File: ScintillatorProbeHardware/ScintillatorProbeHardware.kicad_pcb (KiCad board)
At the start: 2 copper layers, 100 x 100 mm, 116 parts, among them J2 Conn_01x02, J3 Conn_01x03, J4 Conn_01x04, J7 Conn_01x02, Q1 15N10, Q2 S8050, Q3 S8050, Q4 AO401, Q5 S8050, Q6 S8050, Q7 S8050, T1 24:1800, U1 ICL7660, U3 LM358, U4 STM32F103C8Tx, U5 USBLC6-2SC6, U6 AMS1117-3.3, U7 LM318N, U8 LM318N, U9 LM318N, Y1 32.768kHz, Y2 8MHz

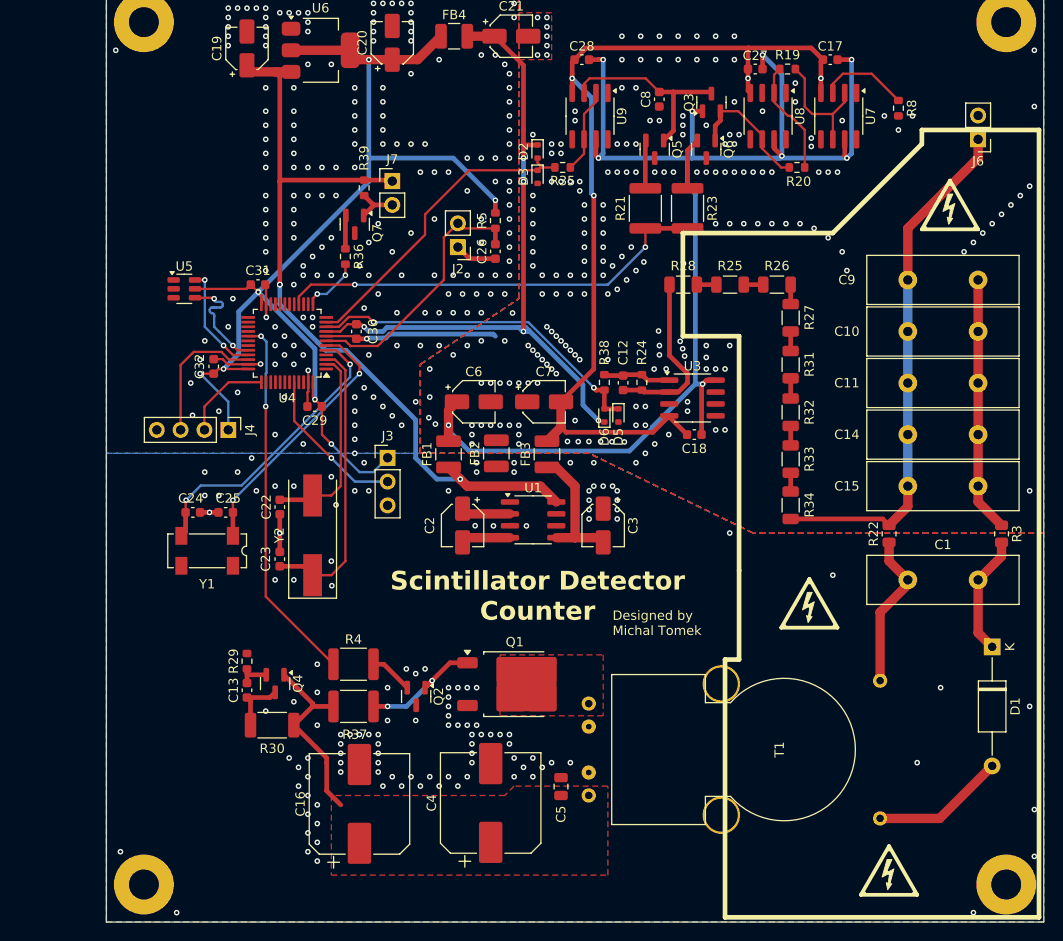
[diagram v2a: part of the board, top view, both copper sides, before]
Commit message: Added USB connector, some loops on PCB optimized
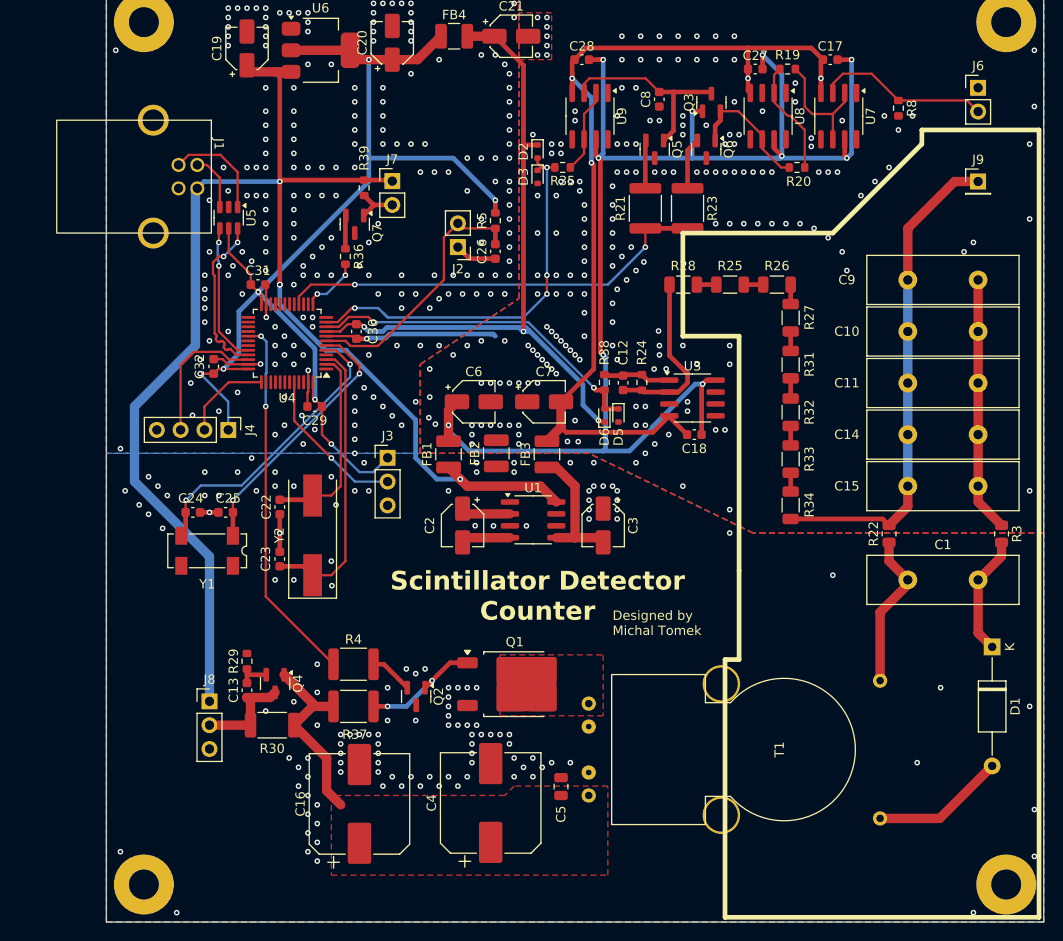
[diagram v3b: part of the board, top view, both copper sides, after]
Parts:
- removed REF** (x7): Symbol_HighVoltage_Triangle_6x6mm_Copper, Symbol:Symbol_HighVoltage_Triangle_6x6mm_Copper
- added J1: USB_B, CustomParts:Amphenol_USB_B, F.Cu at (149.7, 75.2)
- added J8: Conn_01x03, Connector_PinHeader_2.54mm:PinHeader_1x03_P2.54mm_Vertical, F.Cu at (153.0, 132.5)
- added J9: Conn_01x01, Connector_PinHeader_2.54mm:PinHeader_1x01_P2.54mm_Vertical, F.Cu at (235.0, 77.0)
- moved U5 8.95 mm to (155.1, 80.9), turned to -90 degrees
- moved J6 5.50 mm to (235.0, 67.0), turned to 0 degrees
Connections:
- J6 pad 1: HT -> GNDA
- U5 pad 1: Net-(J1-D+) -> /usb_P
- U5 pad 3: Net-(J1-D-) -> /usb_N
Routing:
- net +5V: track 84.5 -> 154.4 mm, vias 3 -> 4
- net /usb_P: track 0.00 -> 11.2 mm
- net Peak_Sense: track 33.7 -> 43.0 mm, vias 0 -> 4
- net PMT_Anode: track 9.60 -> 18.6 mm
- net +5VA: track 145.3 -> 152.5 mm, vias 9 -> 10
- net USB_D+: track 11.9 -> 18.0 mm
- net /usb_N: track 0.00 -> 6.09 mm
- net HT_Power: track 6.33 -> 10.7 mm
- net USB_D-: track 11.9 -> 15.1 mm
- net HT: track 55.9 -> 52.9 mm
- net +3.3V: track 124.1 -> 124.9 mm
- net GNDA: vias 209 -> 200
- net GND: vias 310 -> 334
- net +3.3VA: vias 5 -> 3

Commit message: Hardware finisnig touches, Software directory typo fixed
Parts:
- removed J5: ~, Connector_PinHeader_2.54mm:PinHeader_1x02_P2.54mm_Vertical
- removed R1, R2: 620k, Resistor_SMD:R_1218_3246Metric
- removed R10, R11, R12, R13, R14, R15, R16, R17, R18, R6, R9: 240k, Resistor_SMD:R_1206_3216Metric
- removed R7: 336k, Resistor_SMD:R_1206_3216Metric
- removed V1: ~, CustomParts:BDEG4-42A
- added J10: Conn_01x04, Connector_PinHeader_2.54mm:PinHeader_1x04_P2.54mm_Vertical, F.Cu at (147.5, 89.9)
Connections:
- U4 pad 30: unconnected-(U4-PA9-Pad30) -> UART_TX
- U4 pad 31: unconnected-(U4-PA10-Pad31) -> UART_RX
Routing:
- net UART_RX: track 0.00 -> 11.6 mm, vias 0 -> 1
- net UART_TX: track 0.00 -> 11.2 mm, vias 0 -> 1
- net /usb_P: track 11.2 -> 10.5 mm
- net GNDA: vias 200 -> 224
- net GND: vias 334 -> 361
- net -5VA: vias 4 -> 3
- net (no net): vias 0 -> 1

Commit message: Hardware revision 1 as sent to manifacture
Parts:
- removed Q4: AO401, Package_TO_SOT_SMD:SOT-23
- removed U5: USBLC6-2SC6, Package_TO_SOT_SMD:SOT-23-6
- added C33: 1u, Capacitor_SMD:C_0603_1608Metric, F.Cu at (195.7, 80.2)
- added C34: 1u, Capacitor_SMD:C_0603_1608Metric, F.Cu at (193.0, 80.2)
- added C35: 1u, Capacitor_SMD:C_0603_1608Metric, F.Cu at (223.7, 63.5)
- added C36: 1u, Capacitor_SMD:C_0603_1608Metric, F.Cu at (214.2, 61.2)
- added C37: 1u, Capacitor_SMD:C_0603_1608Metric, F.Cu at (214.0, 76.3)
- added C38: 1u, Capacitor_SMD:C_0603_1608Metric, F.Cu at (203.0, 64.2)
- added Q8: MDD2302, Package_TO_SOT_SMD:SOT-23, F.Cu at (160.6, 138.6)
- added R40: 1k, Resistor_SMD:R_0603_1608Metric, F.Cu at (167.7, 125.5)
- added SYM1: SYM_Flash_Small, CustomParts:W012 - electricity hazard, B.Cu at (228.6, 80.3)
- added SYM2: SYM_Flash_Small, CustomParts:W012 - electricity hazard, B.Cu at (217.0, 120.0)
- added SYM3: SYM_Flash_Small, CustomParts:W012 - electricity hazard, B.Cu at (231.5, 146.0)
- added SYM4: SYM_Flash_Small, CustomParts:W012 - electricity hazard, F.Cu at (228.6, 80.3)
- added SYM5: SYM_Flash_Small, CustomParts:W012 - electricity hazard, F.Cu at (217.0, 120.0)
- added SYM6: SYM_Flash_Small, CustomParts:W012 - electricity hazard, F.Cu at (231.5, 146.0)
- R21, R23: footprint Resistor_SMD:R_1812_4532Metric -> Resistor_SMD:R_0603_1608Metric
- R30: footprint Resistor_SMD:R_2010_5025Metric -> Resistor_SMD:R_0805_2012Metric
- R37, R4: footprint Resistor_SMD:R_1812_4532Metric -> Resistor_SMD:R_2010_5025Metric
- moved R29 12.8 mm to (156.7, 141.0), turned to 180 degrees
- moved R20 12.8 mm to (207.7, 65.5)
- moved C13 7.47 mm to (157.5, 138.7), turned to -90 degrees
- moved R21 2.69 mm to (199.5, 77.2)
- moved R23 2.69 mm to (204.0, 77.2), turned to 90 degrees
- moved R30 1.03 mm to (160.6, 135.5)
- moved R37 0.18 mm to (168.2, 133.0), turned to 180 degrees
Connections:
- C16 pad 1: Net-(Q4-D) -> Net-(Q8-S)
- C4 pad 1: Net-(Q4-D) -> Net-(Q8-S)
- C5 pad 1: Net-(Q4-D) -> Net-(Q8-S)
- J1 pad 2: /usb_N -> USB_D-
- J1 pad 3: /usb_P -> USB_D+
- R20 pad 2: Net-(Q3-B) -> Net-(Q3-E)
- R23 pad 1: Net-(Q6-B) -> Peak_Reset
- R23 pad 2: Peak_Reset -> Net-(Q6-B)
- R30 pad 2: Net-(Q4-D) -> Net-(Q8-S)
- R37 pad 1: Net-(Q4-D) -> Net-(Q1-G)
- R37 pad 2: Net-(Q1-G) -> Net-(Q8-S)
- T1 pad 1: Net-(Q4-D) -> Net-(Q8-S)
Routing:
- net Net-(Q4-D): track 20.3 -> 0.00 mm
- net Net-(Q8-S): track 0.00 -> 19.5 mm
- net +3.3V: track 124.9 -> 136.5 mm, vias 7 -> 8
- net /usb_P: track 10.5 -> 0.00 mm
- net USB_D-: track 15.1 -> 24.8 mm, vias 2 -> 0
- net USB_D+: track 18.0 -> 24.9 mm, vias 2 -> 0
- net /usb_N: track 6.09 -> 0.00 mm
- net Peak_Reset: track 46.5 -> 51.3 mm
- net +5VA: track 152.5 -> 156.4 mm
- net Net-(Q3-B): track 14.0 -> 10.2 mm
- net HT_Drive_Pulse: track 39.6 -> 42.9 mm
- net -5VA: track 96.8 -> 99.8 mm, vias 3 -> 2
- net GNDA: track 45.7 -> 48.1 mm, vias 224 -> 287
- net Net-(Q3-E): track 21.1 -> 23.3 mm
- net HT_Power: track 10.7 -> 12.9 mm
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- added copper zone on F.Cu, net Net-(Q8-S)
- removed copper zone on F.Cu, net Net-(Q4-D)
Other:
- board text added: "Boot"
- board text added: "Buzz"
- board text added: "DANGER High Voltage"
- board text added: "Debug"
- board text added: "Reset"
- board text added: "Revision 1 2025"
- board text added: "UART"
